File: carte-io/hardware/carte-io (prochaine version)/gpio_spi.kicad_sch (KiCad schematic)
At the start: 32 parts, among them J20 Conn_02x08_Odd_Even, J22 JST_PH_B6B, U22 CM1293A-04SO, U23 74LVC125APW, U24 CM1293A-04SO, U25 74LVC125APW, U30 74LVC125APW,118, U31 CM1293A-04SO, U32 74LVC2G125DP,125, U34 CM1293A-04SO

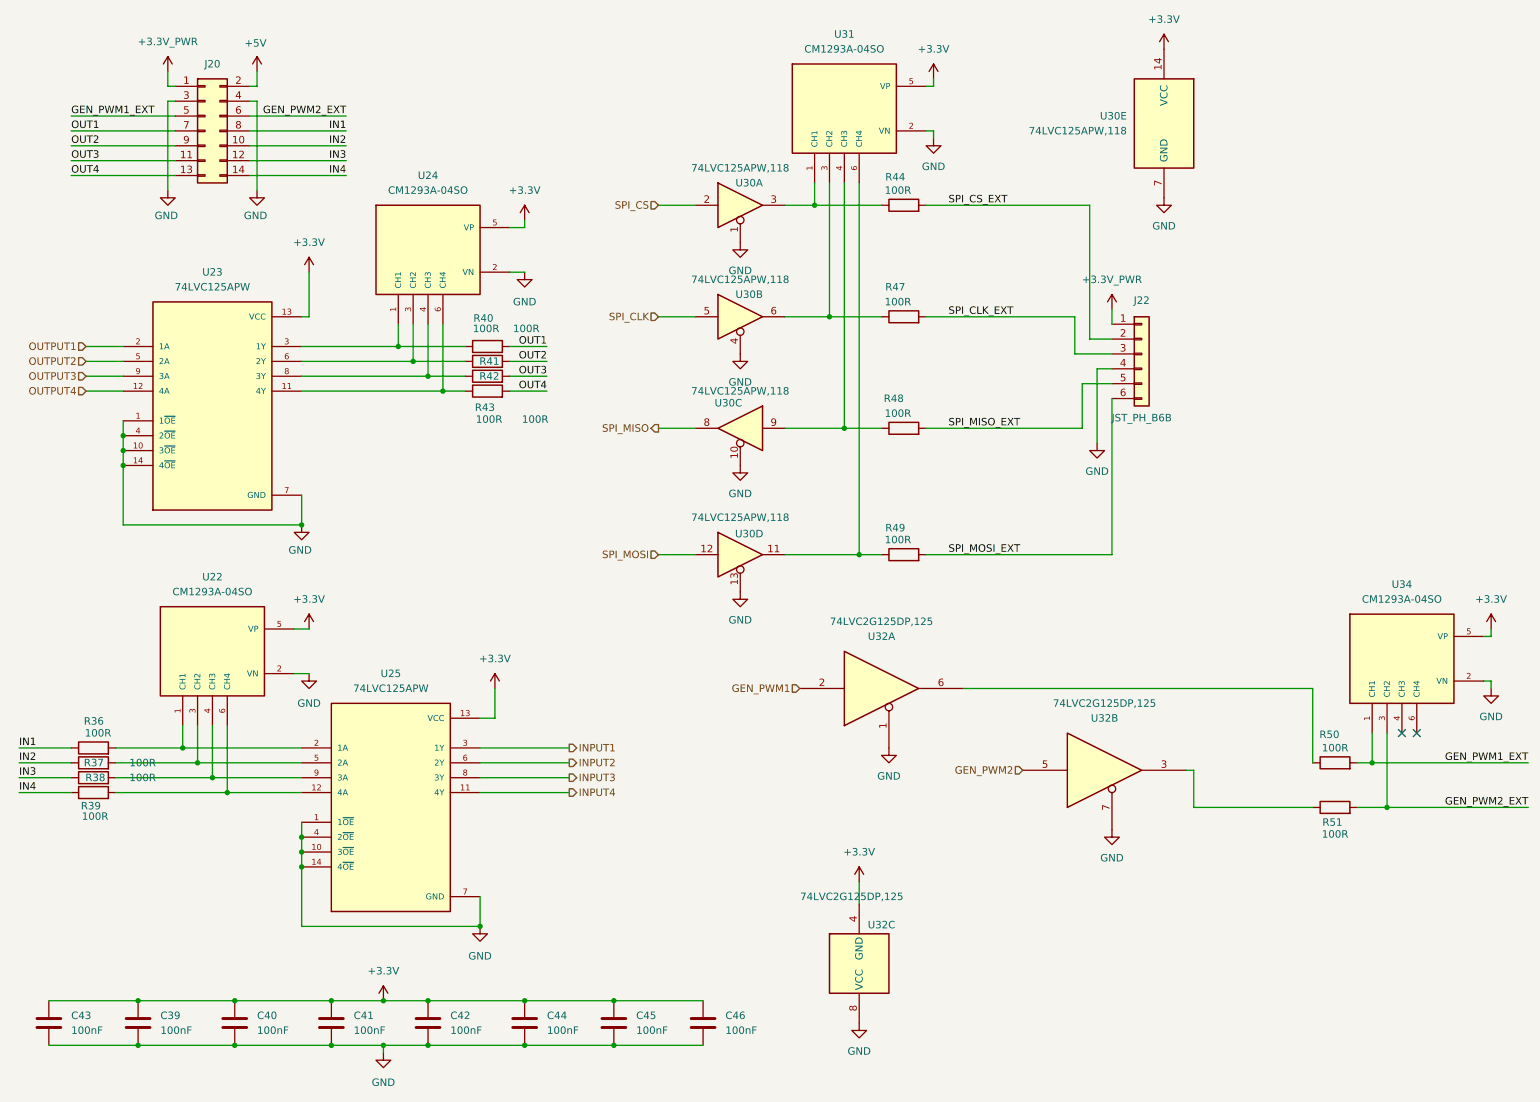
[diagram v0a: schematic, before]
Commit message: Commit de sauvegarde, gros changement sur la carte IO, les connecteurs sont compatibles SeeedStudio Grove. Il faut reprendre une grosse partie du routage et rajouter deux entrées analogiques
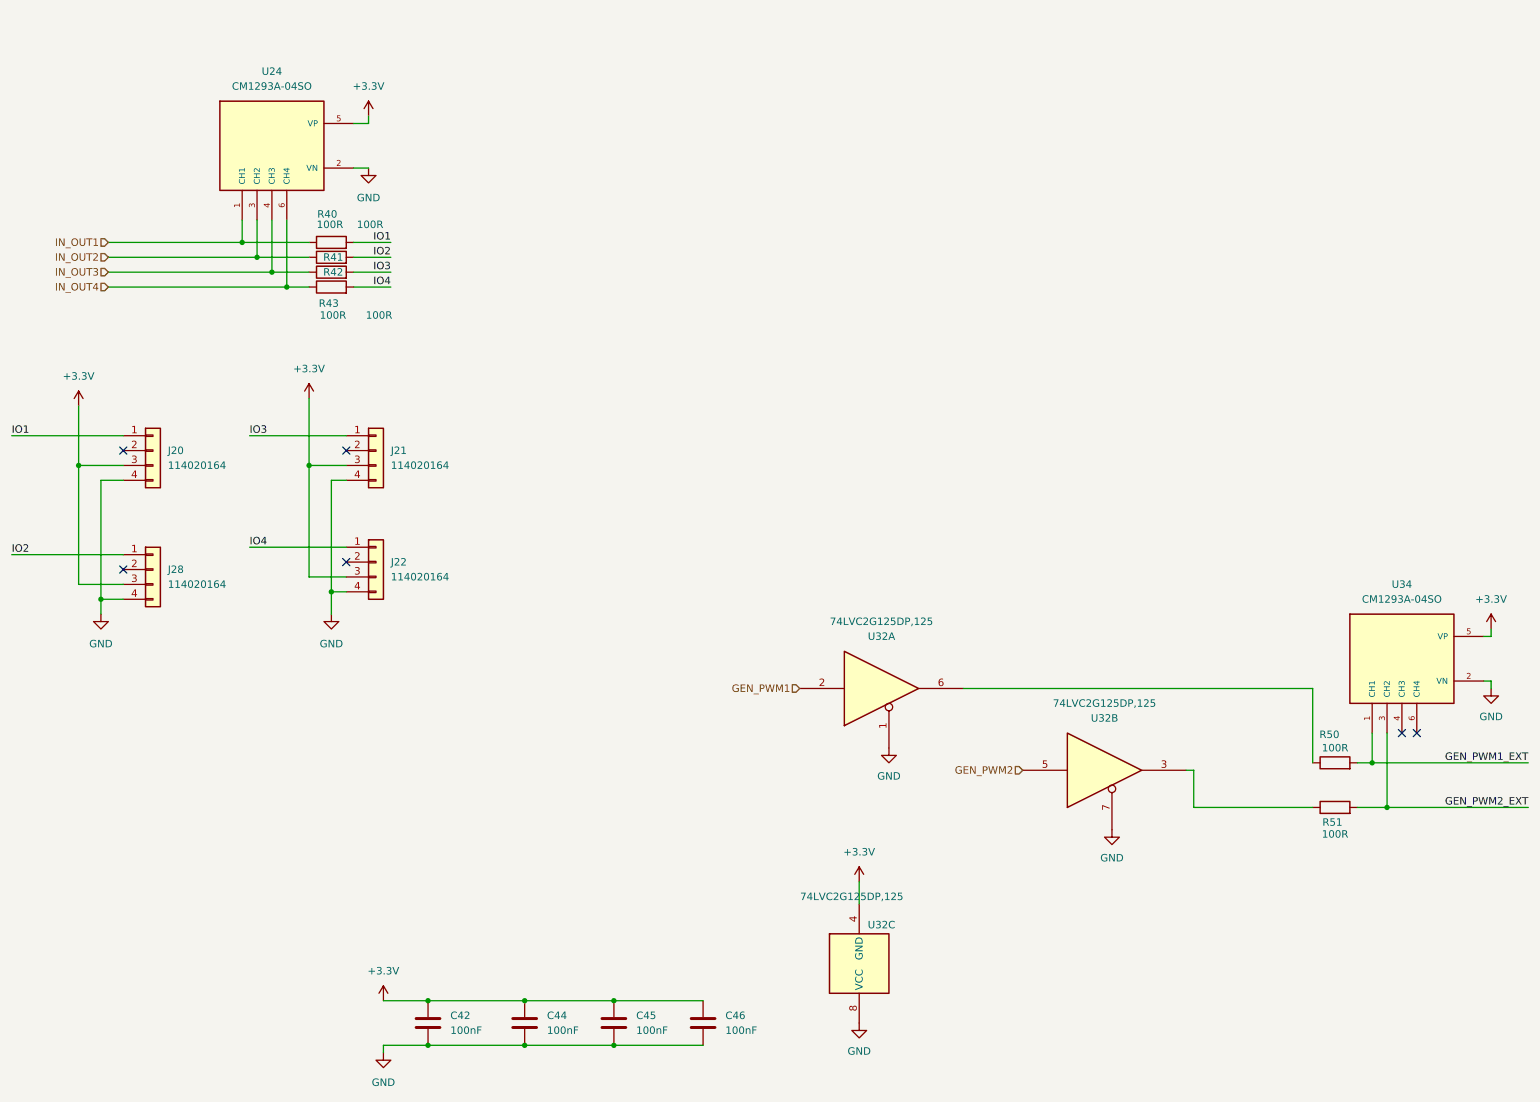
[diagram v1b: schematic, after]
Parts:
- removed C39, C40, C41, C43: 100nF, Capacitor_SMD:C_0805_2012Metric_Pad1.18x1.45mm_HandSolder, symbol Device:C
- removed J20: Conn_02x08_Odd_Even, Connector_PinHeader_2.54mm:PinHeader_2x07_P2.54mm_Vertical, symbol Connector_Generic:Conn_02x07_Odd_Even
- removed J22: JST_PH_B6B, Connector_JST:JST_PH_B6B-PH-K_1x06_P2.00mm_Vertical, symbol Connector_Generic:Conn_01x06
- removed R36, R37, R38, R39, R44, R47, R48, R49: 100R, Resistor_SMD:R_0805_2012Metric_Pad1.20x1.40mm_HandSolder, symbol Device:R
- removed U22, U31: CM1293A-04SO, CM1293A-04SO:SOT95P285X140-6N, symbol CM1293A-04SO:CM1293A-04SO
- removed U23, U25: 74LVC125APW, 74LVC125APW:IC_74LVC125APW, symbol 74LVC125APW:74LVC125APW
- removed U30: 74LVC125APW,118, Package_SO:TSSOP-14_4.4x5mm_P0.65mm, symbol 74xx:74LVC125
- added J20, J21, J22, J28: 114020164, SeeedStudio - Horizontal Header -114020164:SEEEDSTUDIO_114020164, symbol SeeedStudio - Horizontal header:SeeedStudio - 114020164 - R/A
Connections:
- net +3.3V: now also J20.3 (Pin_3), J21.3 (Pin_3), J22.3 (Pin_3), J28.3 (Pin_3)
- net GND: now also J20.4 (Pin_4), J21.4 (Pin_4), J22.4 (Pin_4), J28.4 (Pin_4)
- net IN_OUT4: now reaches R43.1, U24.6 (CH4)
- net IN_OUT3: now reaches R42.1, U24.4 (CH3)
- net IN_OUT1: now reaches R40.1, U24.1 (CH1)
- net IN_OUT2: now reaches R41.1, U24.3 (CH2)
- net OUT1 renamed IO1
- net IO1: now also J20.1 (Pin_1)
- net OUT2 renamed IO2
- net IO2: now also J28.1 (Pin_1)
- net OUT3 renamed IO3
- net IO3: now also J21.1 (Pin_1)
- net OUT4 renamed IO4
- net IO4: now also J22.1 (Pin_1)
- no-connect marks 2 -> 6
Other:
- moved on the sheet: R40, R41, R42, R43, U24

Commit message: -- reorganisation de la carte, - rajout des connecteurs seeedstudio grove - Rajout des deux entrées ADC
travail en cours
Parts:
- removed C46: 100nF, Capacitor_SMD:C_0805_2012Metric_Pad1.18x1.45mm_HandSolder, symbol Device:C
- removed R50, R51: 100R, Resistor_SMD:R_0805_2012Metric_Pad1.20x1.40mm_HandSolder, symbol Device:R
- removed U32: 74LVC2G125DP,125, Package_SO:VSSOP-8_2.3x2mm_P0.5mm, symbol 74xGxx:74LVC2G125
- removed U34: CM1293A-04SO, CM1293A-04SO:SOT95P285X140-6N, symbol CM1293A-04SO:CM1293A-04SO
- added D3, D8: BAT54SFILMY, Package_TO_SOT_SMD:SOT-23, symbol Diode:BAT54S
- added J29, J30: 114020164, SeeedStudio - Horizontal Header -114020164:SEEEDSTUDIO_114020164, symbol SeeedStudio - Horizontal header:SeeedStudio - 114020164 - R/A
- added R36, R37: 100R, Resistor_SMD:R_0805_2012Metric_Pad1.20x1.40mm_HandSolder, symbol Device:R
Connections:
- net +3.3V: now also D3.2 (K), D8.2 (K), J29.3 (Pin_3), J30.3 (Pin_3)
- net GND: now also D3.1 (A), D8.1 (A), J29.4 (Pin_4), J30.4 (Pin_4)
- new net: J30.1 (Pin_1), R37.1
- new net ADC_AN1: D3.3 (COM), R36.2
- new net ADC_AN2: D8.3 (COM), R37.2
- new net AN1: J29.1 (Pin_1), R36.1

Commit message: WIP
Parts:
- added C43: 100nF, Capacitor_SMD:C_0805_2012Metric_Pad1.18x1.45mm_HandSolder, symbol Device:C
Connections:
- net +3.3V: now also C43.1
- net GND: now also C43.2
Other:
- moved on the sheet: C42
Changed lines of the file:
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@@
+	)
+	(junction
+		(at 93.98 189.23)
+		(diameter 0)
+		(color 0 0 0 0)
 	)
 	(junction
@@
 	)
 	(junction
+		(at 93.98 181.61)
+		(diameter 0)
+		(color 0 0 0 0)
+	)
+	(junction
 		(at 185.42 87.63)
 		(diameter 0)
@@
 	(wire
 		(pts
+			(xy 93.98 181.61) (xy 107.95 181.61)
+		)
+		(stroke
+			(width 0)
+			(type default)
+		)
+	)
+	(wire
+		(pts
 			(xy 78.74 59.69) (xy 85.09 59.69)
 		)
@@
 	(wire
 		(pts
-			(xy 107.95 189.23) (xy 91.44 189.23)
+			(xy 107.95 189.23) (xy 93.98 189.23)
 		)
 		(stroke
@@
 	(wire
 		(pts
+			(xy 93.98 189.23) (xy 80.01 189.23)
+		)
+		(stroke
+			(width 0)
+			(type default)
+		)
+	)
+	(wire
+		(pts
 			(xy 71.12 90.17) (xy 71.12 78.74)
 		)
@@
 	(wire
 		(pts
-			(xy 91.44 181.61) (xy 107.95 181.61)
+			(xy 80.01 181.61) (xy 93.98 181.61)
 		)
 		(stroke
@@
 	)
 	(symbol
+		(lib_id "Device:C")
+		(at 93.98 185.42 0)
+		(unit 1)
+		(exclude_from_sim no)
+		(in_bom yes)
+		(on_board yes)
+		(dnp no)
+		(fields_autoplaced yes)
+		(property "Reference" "C43"
+			(at 97.79 184.1499 0)
+			(effects
+				(font
+					(size 1.27 1.27)
+				)
+				(justify left)
+			)
+		)
+		(property "Value" "100nF"
+			(at 97.79 186.6899 0)
+			(effects
+				(font
+					(size 1.27 1.27)
+				)
+				(justify left)
+			)
+		)
+		(property "Footprint" "Capacitor_SMD:C_0805_2012Metric_Pad1.18x1.45mm_HandSolder"
+			(at 94.9452 189.23 0)
+			(effects
+				(font
+					(size 1.27 1.27)
+				)
+				(hide yes)
+			)
+		)
+		(property "Datasheet" "~"
+			(at 93.98 185.42 0)
+			(effects
+				(font
+					(size 1.27 1.27)
+				)
+				(hide yes)
+			)
+		)
+		(property "Description" "Unpolarized capacitor"
+			(at 93.98 185.42 0)
+			(effects
+				(font
+					(size 1.27 1.27)
+				)
+				(hide yes)
+			)
+		)
+		(pin "2"
+		)
+		(pin "1"
+		)
+		(instances
+			(project "carte-io"
+				(path "/acbeee85-bee7-482c-b859-0ad6bf15d6be/3f52fbb8-df6a-4282-9d71-7c6a457205c5"
+					(reference "C43")
+					(unit 1)
+				)
+			)
+		)
+	)
+	(symbol
 		(lib_id "power:GND")
 		(at 107.95 190.5 0)
@@
 	(symbol
 		(lib_id "Device:C")
-		(at 91.44 185.42 0)
+		(at 80.01 185.42 0)
 		(unit 1)
 		(exclude_from_sim no)
@@
 		(fields_autoplaced yes)
 		(property "Reference" "C42"
-			(at 95.25 184.1499 0)
+			(at 83.82 184.1499 0)
 			(effects
 				(font
@@
 		)
 		(property "Value" "100nF"
-			(at 95.25 186.6899 0)
+			(at 83.82 186.6899 0)
 			(effects
 				(font
@@
 		)
 		(property "Footprint" "Capacitor_SMD:C_0805_2012Metric_Pad1.18x1.45mm_HandSolder"
-			(at 92.4052 189.23 0)
+			(at 80.9752 189.23 0)
 			(effects
 				(font
@@
 		)
 		(property "Datasheet" "~"
-			(at 91.44 185.42 0)
+			(at 80.01 185.42 0)
 			(effects
 				(font
@@
 		)
 		(property "Description" "Unpolarized capacitor"
-			(at 91.44 185.42 0)
-			(effects
-				(font
+			(at 80.01 185.42 0)
+			(effects
+				(font
